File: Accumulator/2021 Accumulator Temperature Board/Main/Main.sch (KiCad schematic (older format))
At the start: 8 parts, among them J1001 Conn_01x06, J1002 M3, J1003 Conn_01x04, J1004 Conn_01x04, J1005 M3, J1006 M3, J3 M3

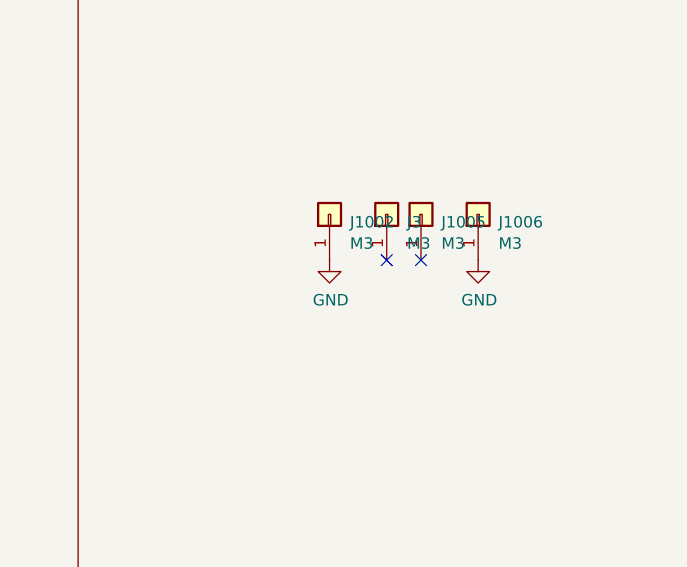
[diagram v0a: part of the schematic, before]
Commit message: Changes to Thermoboard
Disconnected mounting holes from GND, changed Zener package to hand-soldering.
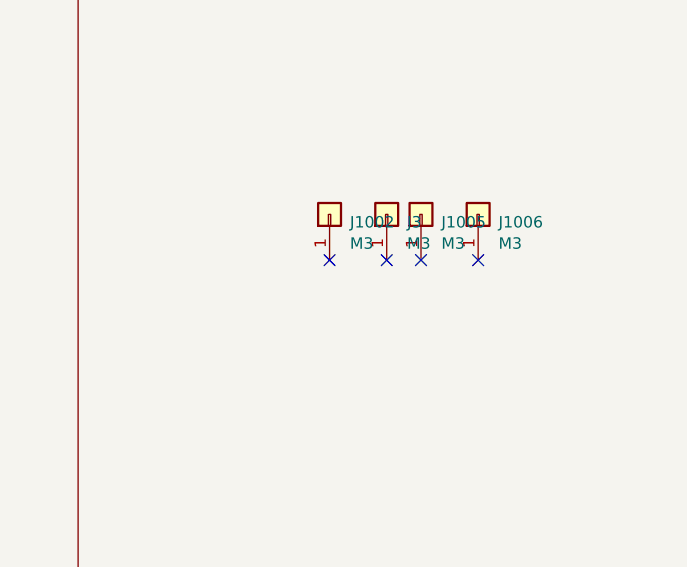
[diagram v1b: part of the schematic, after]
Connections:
- net GND: no longer J1002.1 (Pin_1), J1006.1 (Pin_1)
- no-connect marks 4 -> 6
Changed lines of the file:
@@
-$EndComp
-$Comp
-L power:GND #PWR0149
-U 1 1 5C282761
-P 5150 5350
-F 0 "#PWR0149" H 5150 5100 50  0001 C CNN
-F 1 "GND" H 5155 5175 50  0000 C CNN
-F 2 "" H 5150 5350 50  0001 C CNN
-F 3 "" H 5150 5350 50  0001 C CNN
-	1    5150 5350
-	1    0    0    -1
 $EndComp
 $Comp
@@
 	0    -1   -1   0
 $EndComp
-$Comp
-L power:GND #PWR0161
-U 1 1 5C282FE8
-P 5800 5350
-F 0 "#PWR0161" H 5800 5100 50  0001 C CNN
-F 1 "GND" H 5805 5175 50  0000 C CNN
-F 2 "" H 5800 5350 50  0001 C CNN
-F 3 "" H 5800 5350 50  0001 C CNN
-	1    5800 5350
-	1    0    0    -1
-$EndComp
 NoConn ~ 5550 5350
 NoConn ~ 2300 3000
@@
 $EndComp
 NoConn ~ 5400 5350
+NoConn ~ 5800 5350
+NoConn ~ 5150 5350
 $EndSCHEMATC
